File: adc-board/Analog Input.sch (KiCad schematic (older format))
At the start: 59 parts, among them J1 BHR-44-HUA, U1 Opamp_Quad_Generic, U10 MIC5366-2.0YC5, U2 Opamp_Quad_Generic, U29 AP2114HA-3.3TRG1, U3 Opamp_Quad_Generic, U4 Opamp_Quad_Generic, U5 Opamp_Quad_Generic, U6 Opamp_Quad_Generic

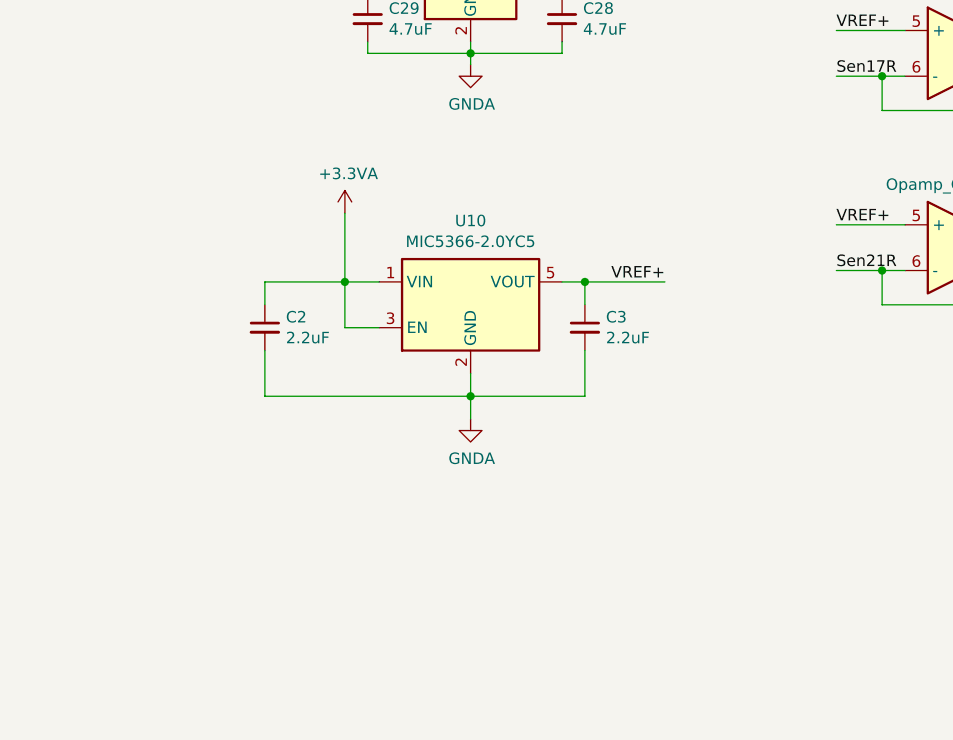
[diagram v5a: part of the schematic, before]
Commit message: Back to the MCP1501 for Vref. Using SOT-23-6 this time.
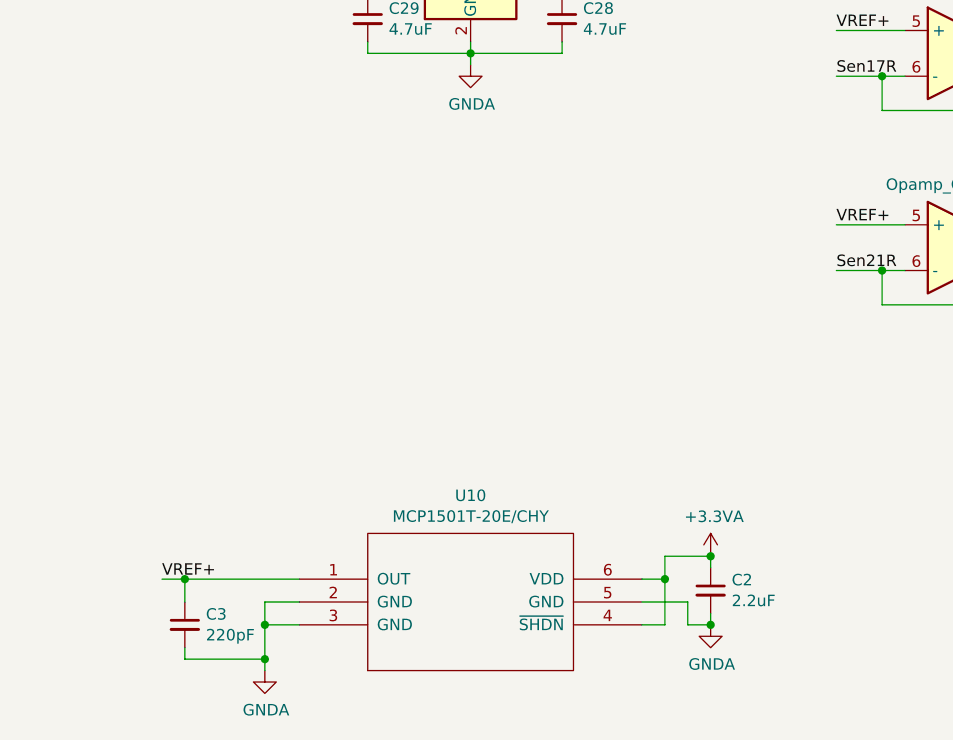
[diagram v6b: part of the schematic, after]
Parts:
- removed U10: MIC5366-2.0YC5, TO_SOT_Packages_SMD:SOT-353_SC-70-5_Handsoldering, symbol Regulator_Linear:MIC5366-3.3YC5
- added U10: MCP1501T-20E/CHY, TO_SOT_Packages_SMD:SOT-23-6_Handsoldering, symbol MCP1501-ECHY:MCP1501-ECHY
- C3: value 2.2uF -> 220pF
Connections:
- wire segments 311 -> 316
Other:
- moved on the sheet: C2, C3
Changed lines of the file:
@@
 L power:GNDA #PWR?
 U 1 1 61D87A4F
-P 4950 8450
+P 4050 9550
 AR Path="/61D87A4F" Ref="#PWR?"  Part="1"
 AR Path="/5FA7E425/61D87A4F" Ref="#PWR0126"  Part="1"
-F 0 "#PWR0126" H 4950 8200 50  0001 C CNN
-F 1 "GNDA" H 4955 8277 50  0000 C CNN
-F 2 "" H 4950 8450 50  0001 C CNN
-F 3 "" H 4950 8450 50  0001 C CNN
-	1    4950 8450
+F 0 "#PWR0126" H 4050 9300 50  0001 C CNN
+F 1 "GNDA" H 4055 9377 50  0000 C CNN
+F 2 "" H 4050 9550 50  0001 C CNN
+F 3 "" H 4050 9550 50  0001 C CNN
+	1    4050 9550
 	1    0    0    -1
 $EndComp
@@
 L Device:C_Small C?
 U 1 1 61D87A55
-P 5450 8050
+P 3700 9350
 AR Path="/61D87A55" Ref="C?"  Part="1"
 AR Path="/5FA7E425/61D87A55" Ref="C3"  Part="1"
-F 0 "C3" H 5542 8096 50  0000 L CNN
-F 1 "2.2uF" H 5542 8005 50  0000 L CNN
-F 2 "Capacitors_SMD:C_0805" H 5450 8050 50  0001 C CNN
-F 3 "~" H 5450 8050 50  0001 C CNN
-	1    5450 8050
+F 0 "C3" H 3792 9396 50  0000 L CNN
+F 1 "220pF" H 3792 9305 50  0000 L CNN
+F 2 "Capacitors_SMD:C_0805" H 3700 9350 50  0001 C CNN
+F 3 "~" H 3700 9350 50  0001 C CNN
+	1    3700 9350
 	1    0    0    -1
 $EndComp
@@
 L Device:C_Small C?
 U 1 1 61D87A5B
-P 4050 8050
+P 6000 9200
 AR Path="/61D87A5B" Ref="C?"  Part="1"
 AR Path="/5FA7E425/61D87A5B" Ref="C2"  Part="1"
-F 0 "C2" H 4142 8096 50  0000 L CNN
-F 1 "2.2uF" H 4142 8005 50  0000 L CNN
-F 2 "Capacitors_SMD:C_0805" H 4050 8050 50  0001 C CNN
-F 3 "~" H 4050 8050 50  0001 C CNN
-	1    4050 8050
+F 0 "C2" H 6092 9246 50  0000 L CNN
+F 1 "2.2uF" H 6092 9155 50  0000 L CNN
+F 2 "Capacitors_SMD:C_0805" H 6000 9200 50  0001 C CNN
+F 3 "~" H 6000 9200 50  0001 C CNN
+	1    6000 9200
 	1    0    0    -1
 $EndComp
@@
 L power:+3.3VA #PWR?
 U 1 1 61D87A61
-P 4400 7550
+P 6000 9050
 AR Path="/61D87A61" Ref="#PWR?"  Part="1"
 AR Path="/5FA7E425/61D87A61" Ref="#PWR0127"  Part="1"
-F 0 "#PWR0127" H 4400 7400 50  0001 C CNN
-F 1 "+3.3VA" H 4415 7723 50  0000 C CNN
-F 2 "" H 4400 7550 50  0001 C CNN
-F 3 "" H 4400 7550 50  0001 C CNN
-	1    4400 7550
+F 0 "#PWR0127" H 6000 8900 50  0001 C CNN
+F 1 "+3.3VA" H 6015 9223 50  0000 C CNN
+F 2 "" H 6000 9050 50  0001 C CNN
+F 3 "" H 6000 9050 50  0001 C CNN
+	1    6000 9050
 	1    0    0    -1
 $EndComp
-$Comp
-L Regulator_Linear:MIC5366-3.3YC5 U?
-U 1 1 61D87A67
-P 4950 7950
-AR Path="/61D87A67" Ref="U?"  Part="1"
-AR Path="/5FA7E425/61D87A67" Ref="U10"  Part="1"
-F 0 "U10" H 4950 8317 50  0000 C CNN
-F 1 "MIC5366-2.0YC5" H 4950 8226 50  0000 C CNN
-F 2 "TO_SOT_Packages_SMD:SOT-353_SC-70-5_Handsoldering" H 4950 8300 50  0001 C CNN
-F 3 "http://ww1.microchip.com/downloads/en/DeviceDoc/mic5365.pdf" H 4650 8750 50  0001 C CNN
-	1    4950 7950
-	1    0    0    -1
-$EndComp
-Wire Wire Line
-	4550 8050 4400 8050
-Wire Wire Line
-	4400 8050 4400 7850
-Wire Wire Line
-	4400 7850 4550 7850
-Wire Wire Line
-	4400 7850 4400 7550
-Connection ~ 4400 7850
-Wire Wire Line
-	5350 7850 5450 7850
-Text Label 5800 7850 2    50   ~ 0
-VREF+
-Wire Wire Line
-	4050 7950 4050 7850
-Wire Wire Line
-	4050 7850 4400 7850
-Wire Wire Line
-	4050 8150 4050 8350
-Wire Wire Line
-	4050 8350 4950 8350
-Wire Wire Line
-	5450 8350 5450 8150
-Wire Wire Line
-	5450 7950 5450 7850
-Connection ~ 5450 7850
-Wire Wire Line
-	5450 7850 5800 7850
-Wire Wire Line
-	4950 8250 4950 8350
-Connection ~ 4950 8350
-Wire Wire Line
-	4950 8350 5450 8350
-Wire Wire Line
-	4950 8350 4950 8450
+Text Label 3600 9150 0    50   ~ 0
+VREF+
 Connection ~ 7500 5150
 Wire Wire Line
@@
 Text Label 4400 5450 2    50   ~ 0
 VREF+
+$Comp
+L MCP1501-ECHY:MCP1501-ECHY U10
+U 1 1 6008792F
+P 4950 9250
+F 0 "U10" H 4950 9715 50  0000 C CNN
+F 1 "MCP1501T-20E/CHY" H 4950 9624 50  0000 C CNN
+F 2 "TO_SOT_Packages_SMD:SOT-23-6_Handsoldering" H 4950 9250 50  0001 C CNN
+F 3 "DOCUMENTATION" H 4950 9250 50  0001 C CNN
+	1    4950 9250
+	1    0    0    -1
+$EndComp
+Wire Wire Line
+	4050 9550 4050 9500
+Wire Wire Line
+	4050 9250 4200 9250
+Wire Wire Line
+	4200 9350 4050 9350
+Connection ~ 4050 9350
+Wire Wire Line
+	4050 9350 4050 9250
+Wire Wire Line
+	4200 9150 3700 9150
+Wire Wire Line
+	3700 9250 3700 9150
+Connection ~ 3700 9150
+Wire Wire Line
+	3700 9150 3600 9150
+Wire Wire Line
+	3700 9450 3700 9500
+Wire Wire Line
+	3700 9500 4050 9500
+Connection ~ 4050 9500
+Wire Wire Line
+	4050 9500 4050 9350
+Wire Wire Line
+	5700 9150 5800 9150
+Wire Wire Line
+	5800 9150 5800 9050
+Wire Wire Line
+	5800 9050 6000 9050
+Wire Wire Line
+	6000 9050 6000 9100
+Wire Wire Line
+	5700 9350 5800 9350
+Wire Wire Line
+	5800 9350 5800 9150
+Connection ~ 5800 9150
+Wire Wire Line
+	5700 9250 5900 9250
+Wire Wire Line
+	5900 9250 5900 9350
+Wire Wire Line
+	5900 9350 6000 9350
+Wire Wire Line
+	6000 9350 6000 9300
+$Comp
+L power:GNDA #PWR?
+U 1 1 60182CE5
+P 6000 9350
+AR Path="/60182CE5" Ref="#PWR?"  Part="1"
+AR Path="/5FA7E425/60182CE5" Ref="#PWR0119"  Part="1"
+F 0 "#PWR0119" H 6000 9100 50  0001 C CNN
+F 1 "GNDA" H 6005 9177 50  0000 C CNN
+F 2 "" H 6000 9350 50  0001 C CNN
+F 3 "" H 6000 9350 50  0001 C CNN
+	1    6000 9350
+	1    0    0    -1
+$EndComp
+Connection ~ 6000 9350
+Connection ~ 6000 9050
 $EndSCHEMATC
